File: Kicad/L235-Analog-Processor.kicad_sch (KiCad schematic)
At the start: 300 parts, among them J1 Input A, J10 Half Wave A + -B, J11 Inverted Out B, J12 CV Select, J13 CV Select, J14 Conn_01x20_Pin, J15 Inverted Out A, J16 Full-Wave Rectifier A, J17 Half-Wave Rectifier A, J18 √(A²+B²), J19 Conn_01x20_Socket, J2 Input B, J3 Function IN, J4 ( 10A / |B| ) / ( A * B / 10 ), J5 Output F(x), J6 Power, J7 Full-Wave Rectifier B, J8 A - B, J9 Negative Half-Wave Rectifier B, U1 TL082, U10 TL082, U11 TL082, U12 TL082, U13 TL084, U14 RC4580, U15 TL082, U16 AD633ARZ-RL, U17 TL082, U18 LM4040DBZ-10, U19 74HC148, U2 TL082, U20 LM339, U21 LM339, U22 DG4051E, U23 DG4051E, U24 DG4051E, U25 DG4051E, U26 DG4051E, U27 74LS151, U28 DG4051E, U29 LM339, U3 TL082, U30 LM339, U31 74HC148, U32 DG4051E, U33 DG4051E, U34 DG4051E, U35 DG4051E, U36 LM78M05_TO252, U37 TL082, U4 TL082, U5 TL082, U6 TL082, U7 TL082, U8 TL082, U9 TL082

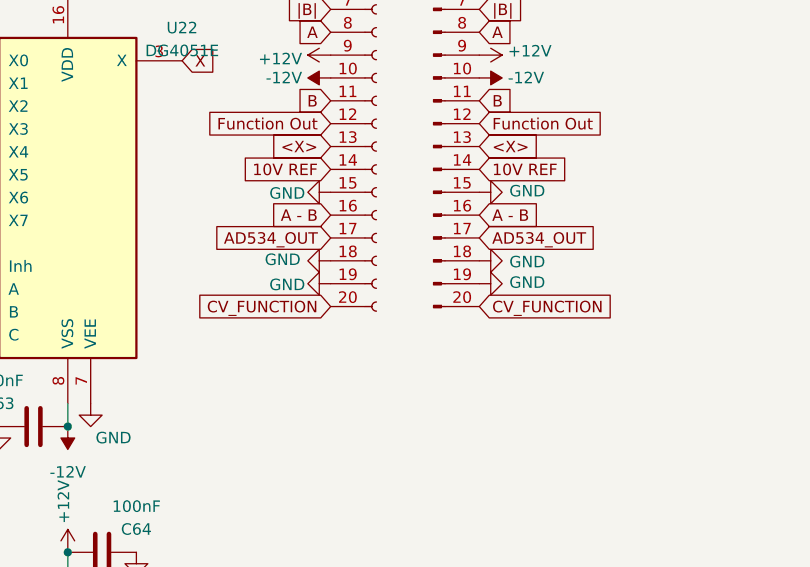
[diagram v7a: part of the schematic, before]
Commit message: Fixed missing routing voltage/gnd
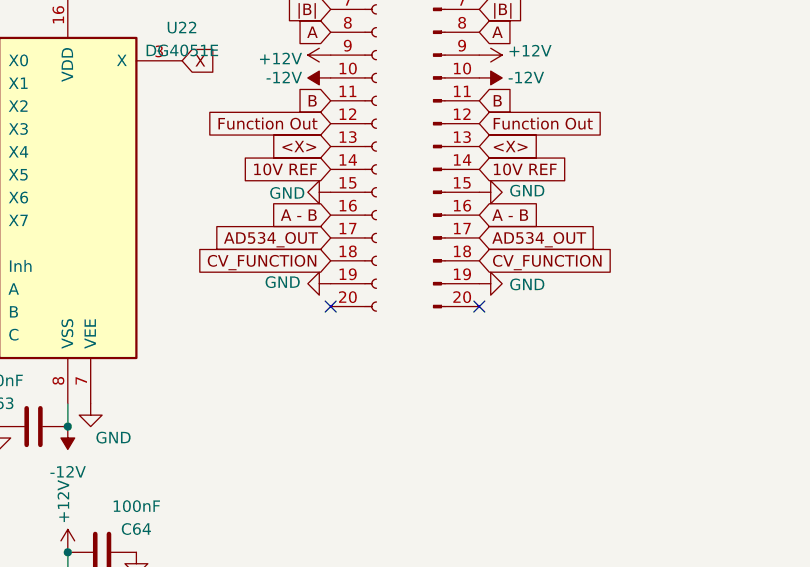
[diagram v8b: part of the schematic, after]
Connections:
- net CV_FUNCTION: now also J14.18 (Pin_18), J19.18 (Pin_18); no longer J14.20 (Pin_20), J19.20 (Pin_20)
- net GND: no longer J14.18 (Pin_18), J19.18 (Pin_18)
- no-connect marks 50 -> 52
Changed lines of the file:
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@@
   (no_connect (at 71.12 593.09))
   (no_connect (at 154.94 247.015))
+  (no_connect (at 214.63 544.195))
   (no_connect (at 398.78 95.885))
   (no_connect (at 168.275 178.435))
@@
   (no_connect (at 290.83 607.695))
   (no_connect (at 181.61 450.85))
+  (no_connect (at 198.12 544.195))
   (no_connect (at 401.32 509.27))
   (no_connect (at 401.32 506.73))
@@
     )
   )
-  (global_label "CV_FUNCTION" (shape input) (at 214.63 544.195 0) (fields_autoplaced)
+  (global_label "CV_FUNCTION" (shape input) (at 214.63 539.115 0) (fields_autoplaced)
     (effects (font (size 1.27 1.27)) (justify left))
-    (property "Intersheetrefs" "${INTERSHEET_REFS}" (at 230.1944 544.195 0)
+    (property "Intersheetrefs" "${INTERSHEET_REFS}" (at 230.1944 539.115 0)
       (effects (font (size 1.27 1.27)) (justify left) hide)
     )
@@
     )
   )
-  (global_label "CV_FUNCTION" (shape input) (at 198.12 544.195 180) (fields_autoplaced)
+  (global_label "CV_FUNCTION" (shape input) (at 198.12 539.115 180) (fields_autoplaced)
     (effects (font (size 1.27 1.27)) (justify right))
-    (property "Intersheetrefs" "${INTERSHEET_REFS}" (at 182.5556 544.195 0)
+    (property "Intersheetrefs" "${INTERSHEET_REFS}" (at 182.5556 539.115 0)
       (effects (font (size 1.27 1.27)) (justify right) hide)
     )
@@
     )
   )
-  (symbol (lib_id "power:GND") (at 198.12 541.655 270) (unit 1)
-    (in_bom yes) (on_board yes) (dnp no)
-    (property "Reference" "#PWR0187" (at 191.77 541.655 0)
-      (effects (font (size 1.27 1.27)) hide)
-    )
-    (property "Value" "GND" (at 193.294 541.782 90)
-      (effects (font (size 1.27 1.27)))
-    )
-    (property "Footprint" "" (at 198.12 541.655 0)
-      (effects (font (size 1.27 1.27)) hide)
-    )
-    (property "Datasheet" "" (at 198.12 541.655 0)
-      (effects (font (size 1.27 1.27)) hide)
-    )
-    (pin "1")
-    (instances
-      (project "L235-Analog-Processor"
-        (path "/11565f7a-671a-4a91-8d3b-c6d6401f938b"
-          (reference "#PWR0187") (unit 1)
-        )
-      )
-    )
-  )
   (symbol (lib_id "Device:C") (at 319.532 354.33 180) (unit 1)
     (in_bom yes) (on_board yes) (dnp no)
@@
     )
   )
-  (symbol (lib_id "power:GND") (at 214.63 541.655 90) (unit 1)
-    (in_bom yes) (on_board yes) (dnp no)
-    (property "Reference" "#PWR0188" (at 220.98 541.655 0)
-      (effects (font (size 1.27 1.27)) hide)
-    )
-    (property "Value" "GND" (at 219.964 541.528 90)
-      (effects (font (size 1.27 1.27)))
-    )
-    (property "Footprint" "" (at 214.63 541.655 0)
-      (effects (font (size 1.27 1.27)) hide)
-    )
-    (property "Datasheet" "" (at 214.63 541.655 0)
-      (effects (font (size 1.27 1.27)) hide)
-    )
-    (pin "1")
-    (instances
-      (project "L235-Analog-Processor"
-        (path "/11565f7a-671a-4a91-8d3b-c6d6401f938b"
-          (reference "#PWR0188") (unit 1)
-        )
-      )
-    )
-  )
   (symbol (lib_id "power:GND") (at 222.25 85.725 0) (unit 1)
     (in_bom yes) (on_board yes) (dnp no) (fields_autoplaced)
@@
     )
   )
-  (symbol (lib_id "power:GND") (at 198.12 539.115 270) (unit 1)
+  (symbol (lib_id "power:GND") (at 198.12 541.655 270) (unit 1)
     (in_bom yes) (on_board yes) (dnp no)
-    (property "Reference" "#PWR0186" (at 191.77 539.115 0)
+    (property "Reference" "#PWR0186" (at 191.77 541.655 0)
       (effects (font (size 1.27 1.27)) hide)
     )
-    (property "Value" "GND" (at 192.786 538.988 90)
+    (property "Value" "GND" (at 192.786 541.528 90)
       (effects (font (size 1.27 1.27)))
     )
-    (property "Footprint" "" (at 198.12 539.115 0)
+    (property "Footprint" "" (at 198.12 541.655 0)
       (effects (font (size 1.27 1.27)) hide)
     )
-    (property "Datasheet" "" (at 198.12 539.115 0)
+    (property "Datasheet" "" (at 198.12 541.655 0)
       (effects (font (size 1.27 1.27)) hide)
     )
@@
     )
   )
-  (symbol (lib_id "power:GND") (at 214.63 539.115 90) (unit 1)
+  (symbol (lib_id "power:GND") (at 214.63 541.655 90) (unit 1)
     (in_bom yes) (on_board yes) (dnp no)
-    (property "Reference" "#PWR0183" (at 220.98 539.115 0)
+    (property "Reference" "#PWR0183" (at 220.98 541.655 0)
       (effects (font (size 1.27 1.27)) hide)
     )
-    (property "Value" "GND" (at 219.964 539.242 90)
+    (property "Value" "GND" (at 219.964 541.782 90)
       (effects (font (size 1.27 1.27)))
     )
-    (property "Footprint" "" (at 214.63 539.115 0)
+    (property "Footprint" "" (at 214.63 541.655 0)
       (effects (font (size 1.27 1.27)) hide)
     )
-    (property "Datasheet" "" (at 214.63 539.115 0)
+    (property "Datasheet" "" (at 214.63 541.655 0)
       (effects (font (size 1.27 1.27)) hide)
     )
